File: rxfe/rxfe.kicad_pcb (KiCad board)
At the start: 2 copper layers, 117.1 x 30.7 mm, 71 parts, among them J1 SMA, J2 SMA, J3 4610X-AP1-103LF, P1 CONN_10X2, P2 CONN_2, U1 SKY12347, U10 SMP1330-005LF, U11 SMP1330-005LF, U12 SMP1330-005LF, U2 74HC04, U3 SCLF-25, U4 HMC595, U5 HMC595, U6 MGA-61563, U7 MGA-61563, U8 HMC595, U9 HMC595

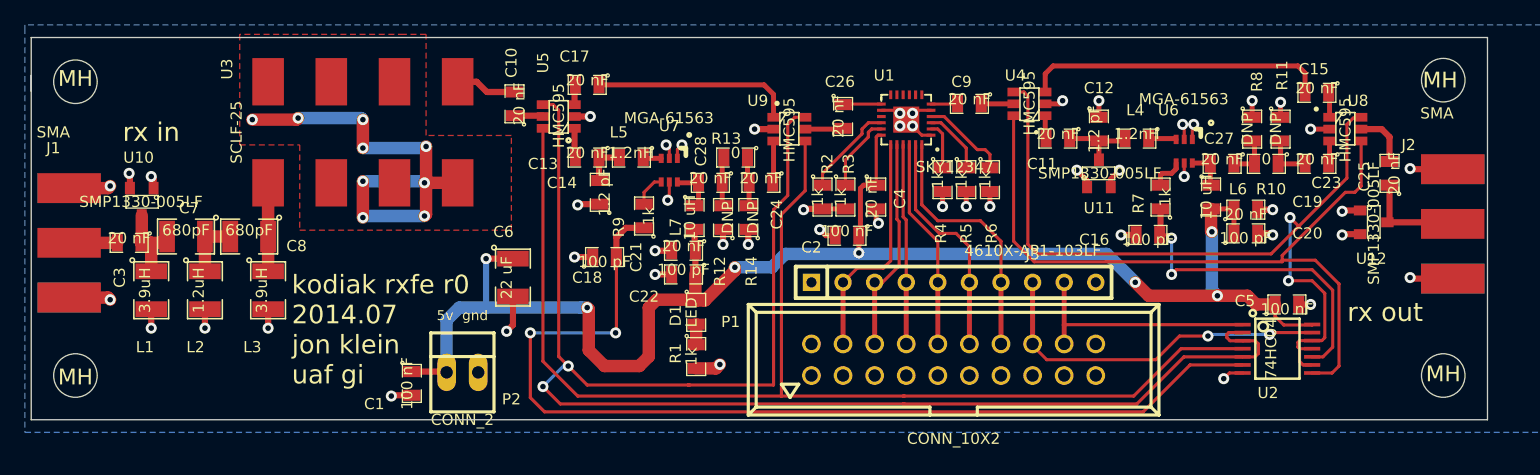
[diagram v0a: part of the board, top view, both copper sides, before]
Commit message: fixed layout bugs on rxfe, changed usrp control header, added 12v->5v linear regulator
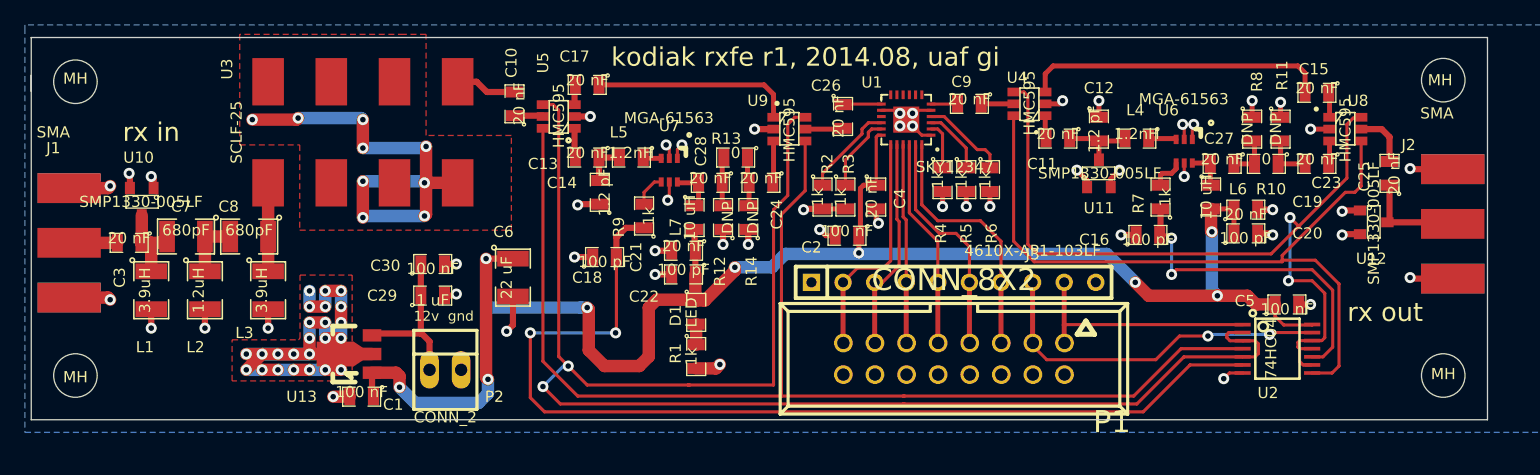
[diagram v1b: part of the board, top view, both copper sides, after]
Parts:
- added C29: 100 nF, SMD_Packages:SMD-0805, F.Cu at (131.3, 108.1)
- added C30: 1 uF, SMD_Packages:SMD-0805, F.Cu at (131.3, 110.7)
- added U13: LM7805, Housings_SOT-89:SOT89-3_Housing, F.Cu at (124.6, 115.4)
- P1: value CONN_10X2 -> CONN_8X2; footprint Connect:VASCH10x2 -> Connect:VASCH8x2
- moved C1 4.18 mm to (125.6, 118.8), turned to 180 degrees
- moved P2 1.39 mm to (132.4, 116.6)
- moved P1 0.08 mm to (173.3, 115.7), turned to 180 degrees
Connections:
- P1 pad 1: (no net) -> /AMP1CTL
- P1 pad 10: Net-(J3-Pad5) -> GND
- P1 pad 11: (no net) -> Net-(J3-Pad4)
- P1 pad 12: Net-(J3-Pad6) -> GND
- P1 pad 13: (no net) -> Net-(J3-Pad3)
- P1 pad 14: Net-(J3-Pad7) -> GND
- P1 pad 15: (no net) -> Net-(J3-Pad2)
- P1 pad 16: /AMP2CTL -> GND
- P1 pad 2: (no net) -> GND
- P1 pad 3: (no net) -> /AMP2CTL
- P1 pad 4: Net-(J3-Pad2) -> GND
- P1 pad 5: (no net) -> Net-(J3-Pad7)
- P1 pad 6: Net-(J3-Pad3) -> GND
- P1 pad 7: (no net) -> Net-(J3-Pad6)
- P1 pad 8: Net-(J3-Pad4) -> GND
- P1 pad 9: (no net) -> Net-(J3-Pad5)
- P2 pad 1: +5V -> Net-(C29-Pad1)
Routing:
- net GND: track 125.9 -> 177.4 mm, vias 59 -> 85
- net +5V: track 124.0 -> 137.5 mm, vias 7 -> 9
- net Net-(C29-Pad1): track 0.00 -> 12.9 mm
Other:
- board text added: "12v gnd"
- board text added: "kodiak rxfe r1 2014.08 jon klein uaf gi"
- board text added: "kodiak rxfe r1, 2014.08, uaf gi"
- board text removed: "5v gnd"
- board text removed: "kodiak rxfe r0 2014.07 jon klein uaf gi"

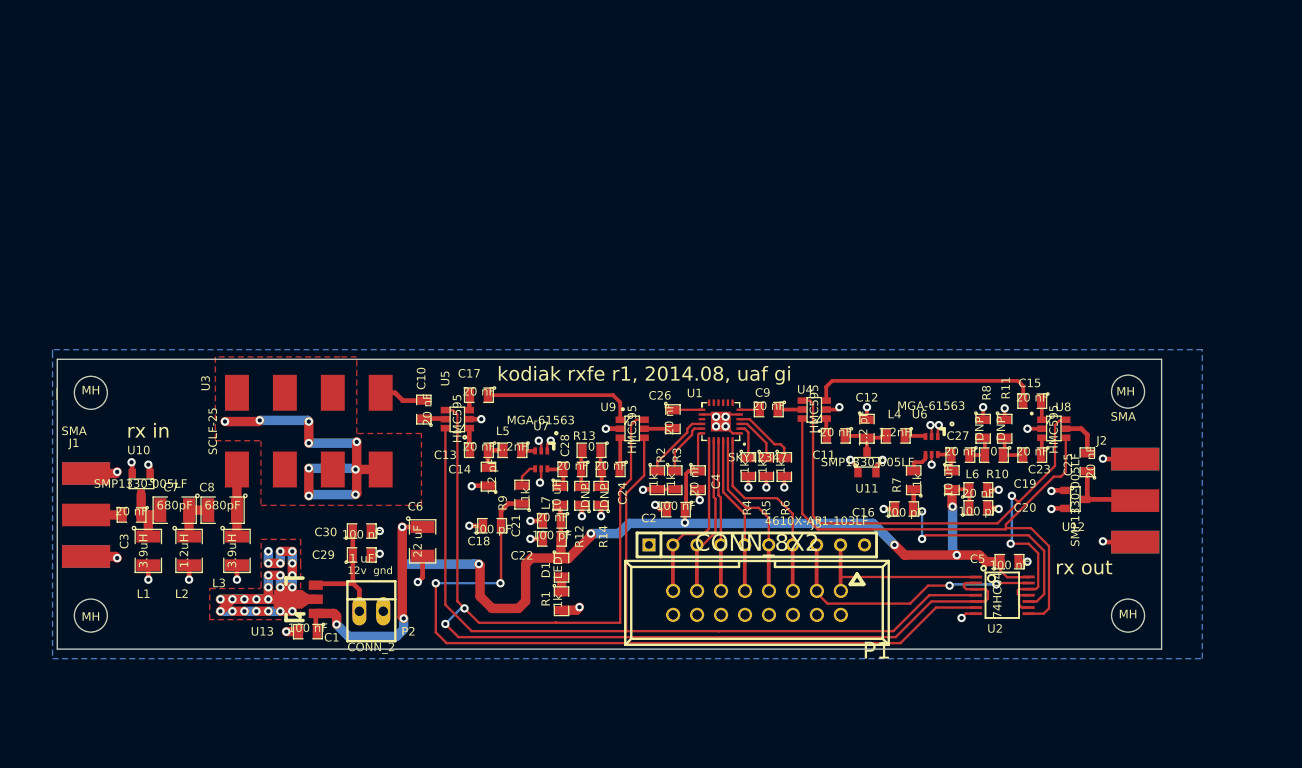
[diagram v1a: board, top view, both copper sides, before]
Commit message: switched to through hole SMA connectors on rxfe and control board, added larger mounting holes for rxfe to mount directly to shelf
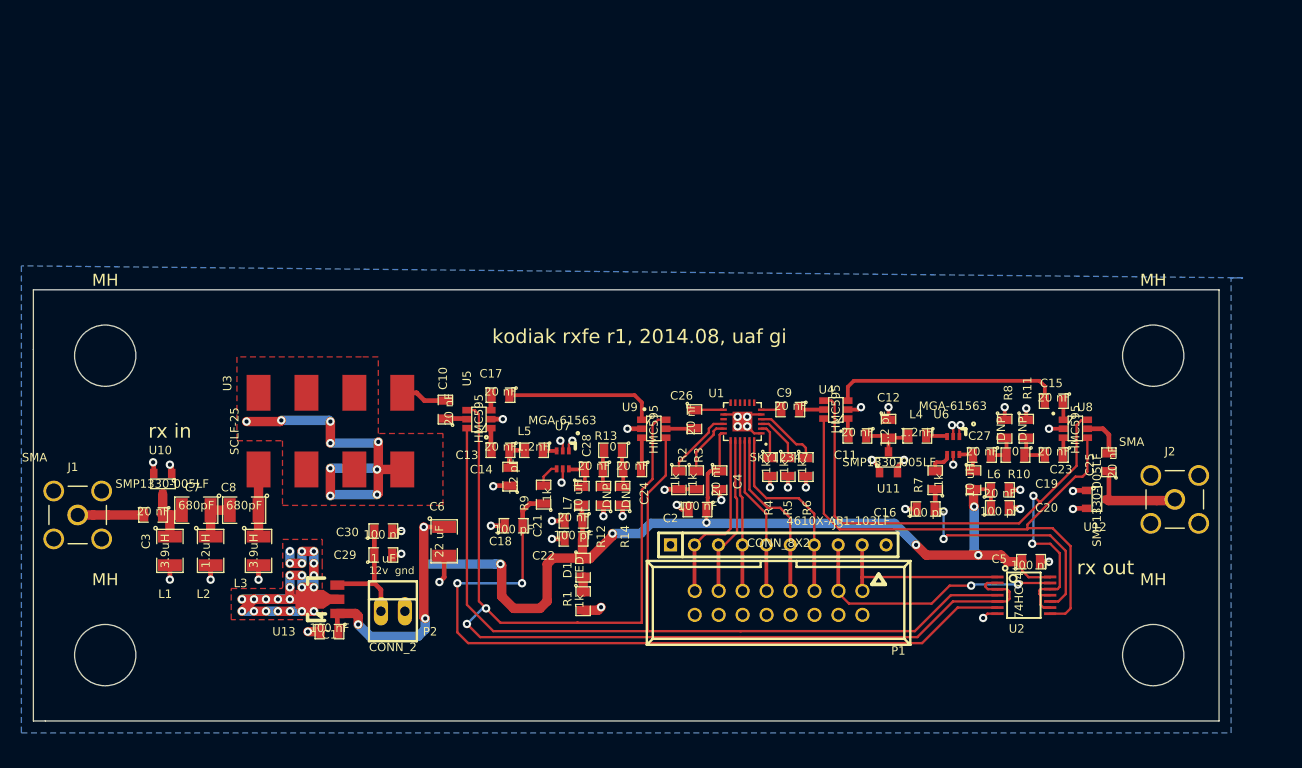
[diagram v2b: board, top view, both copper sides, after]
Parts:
- removed the MH at (212.6, 93.3)
- removed the MH at (212.6, 117.1)
- removed the MH at (102.6, 117.1)
- removed the MH at (102.6, 93.5)
- added MH: MountingHole_6-5mm_RevA_Date21Jun2010, Mounting_Holes:MountingHole_6-5mm, F.Cu at (104.1, 89.5)
- added MH: MountingHole_6-5mm_RevA_Date21Jun2010, Mounting_Holes:MountingHole_6-5mm, F.Cu at (104.1, 121.3)
- added MH: MountingHole_6-5mm_RevA_Date21Jun2010, Mounting_Holes:MountingHole_6-5mm, F.Cu at (215.3, 121.3)
- added MH: MountingHole_6-5mm_RevA_Date21Jun2010, Mounting_Holes:MountingHole_6-5mm, F.Cu at (215.3, 89.5)
- C1: footprint SMD_Packages:SM0805 -> SMD_Packages:SMD-0805
- J1, J2: footprint sma:sma -> local:SMA_5-1814832-1
- moved J2 4.19 mm to (217.6, 104.8)
- moved C1 2.29 mm to (127.9, 118.8)
- moved C10 2.29 mm to (140.2, 95.2)
- moved C12 2.29 mm to (187.2, 97.3)
- moved C13 2.29 mm to (146.1, 99.6)
- moved C14 2.29 mm to (147.1, 102.4)
- moved C15 2.29 mm to (204.7, 94.4)
- moved C16 2.29 mm to (191.1, 105.8)
- moved C17 2.29 mm to (146.1, 93.7)
- moved C18 2.29 mm to (147.4, 107.6)
- moved C2 2.29 mm to (166.9, 105.9)
- moved C21 2.29 mm to (153.8, 107.1)
- moved C22 2.29 mm to (153.8, 109.0)
- moved C23 2.29 mm to (204.7, 100.1)
- moved C24 2.29 mm to (160.0, 101.6)
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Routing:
- net GND: track 177.4 -> 163.8 mm, vias 85 -> 81
- net Net-(C3-Pad2): track 3.87 -> 7.05 mm
- net Net-(C25-Pad1): track 8.36 -> 10.3 mm
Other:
- board size 117.1 x 30.7 mm -> 125.7 x 45.7 mm

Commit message: moved mounting holes on rxfe to match shelf
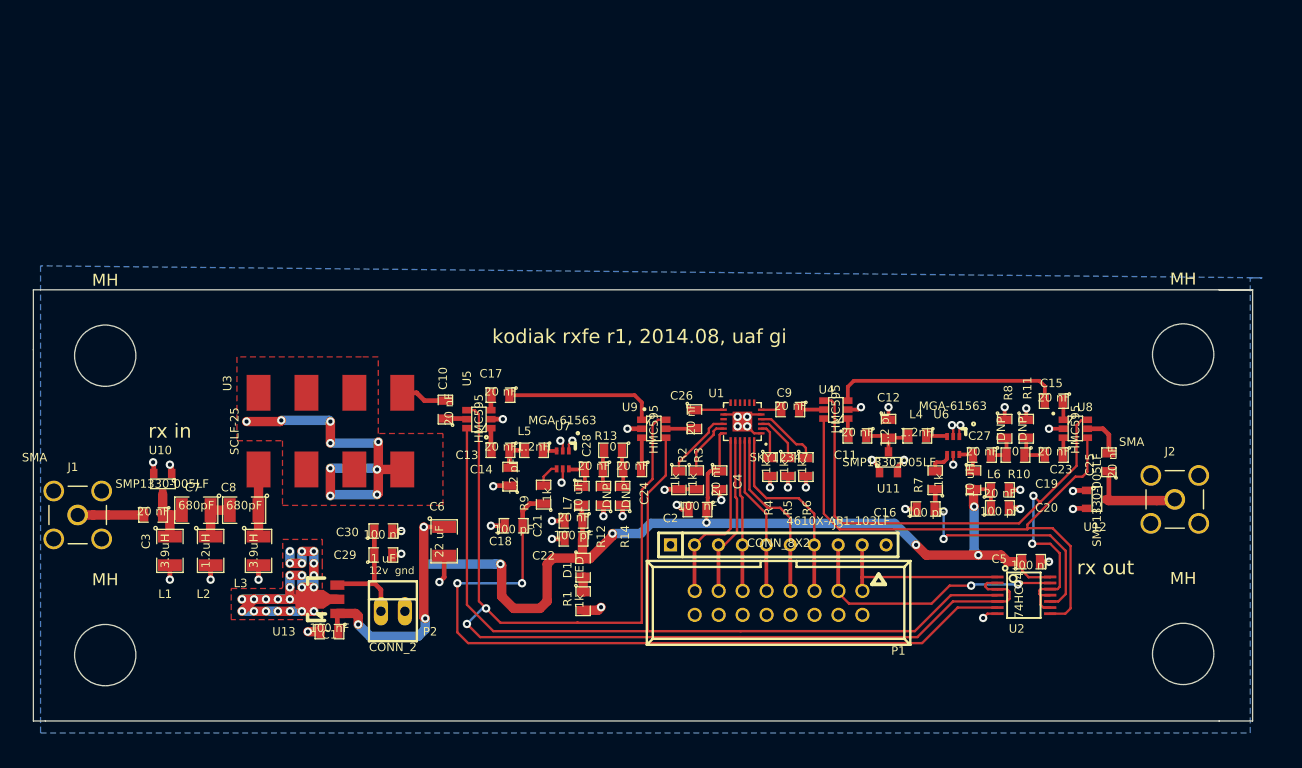
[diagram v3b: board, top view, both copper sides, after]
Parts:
- moved MH 3.18 mm to (218.4, 121.2)
- moved MH 3.18 mm to (218.4, 89.4)
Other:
- board size 125.7 x 45.7 mm -> 129.3 x 45.7 mm

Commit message: switched driver amp current limiter to to-220 lm317hv, heatsink against al plate
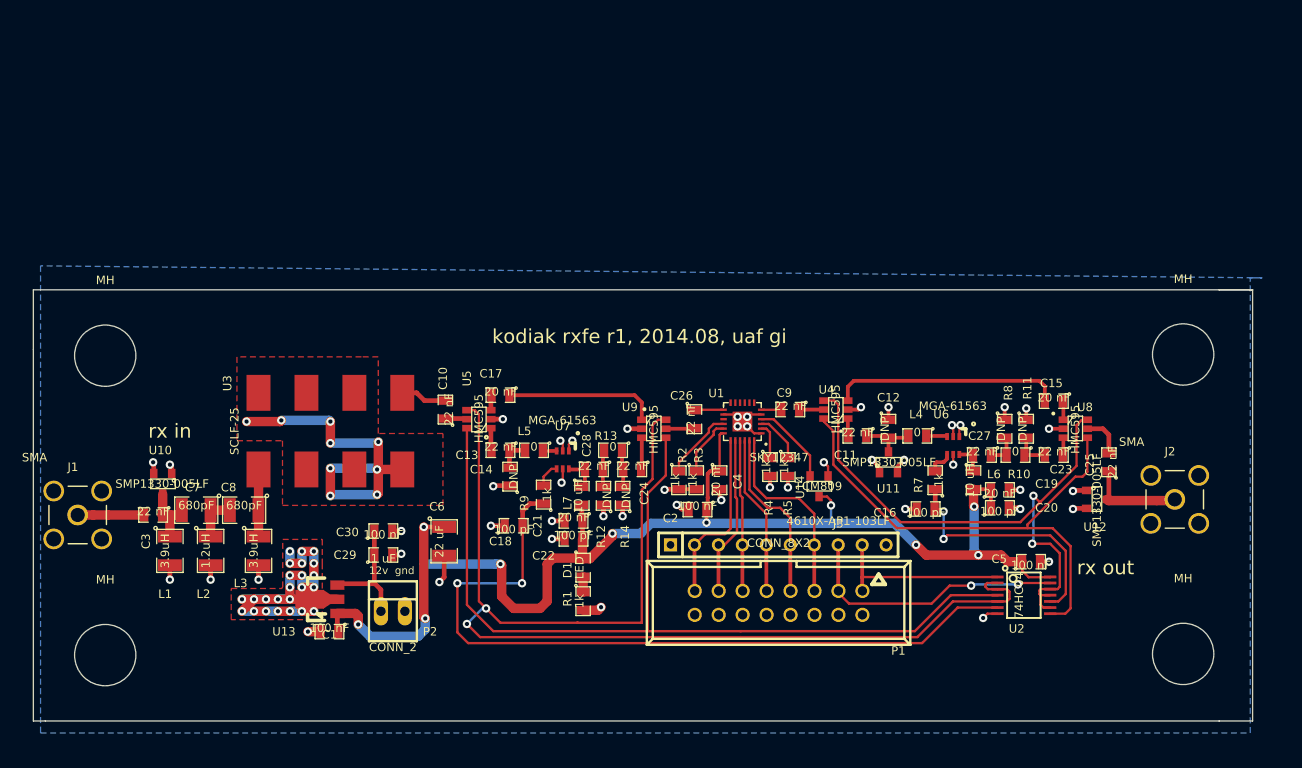
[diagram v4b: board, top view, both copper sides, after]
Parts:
- removed R6: 1k, SMD_Packages:SM0805
- added U14: TCM809, SMD_Packages:SOT-23, F.Cu at (179.8, 103.4)
- C10, C11, C13, C23, C24, C25, C26, C27, C28, C3, C9: value 20 nF -> 22 nF
- C12, C14: value 1.2 pF -> DNP
- L4, L5: value 1.2nH -> 0
- U13: value LM7805 -> 7805
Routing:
- net +5V: track 137.5 -> 141.6 mm, vias 9 -> 10
- net /AMP2: track 59.5 -> 55.7 mm
- net /~AMP2: track 66.7 -> 62.9 mm
- net Net-(U1-Pad4): track 7.07 -> 8.92 mm

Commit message: updated silkscreen on rxfe
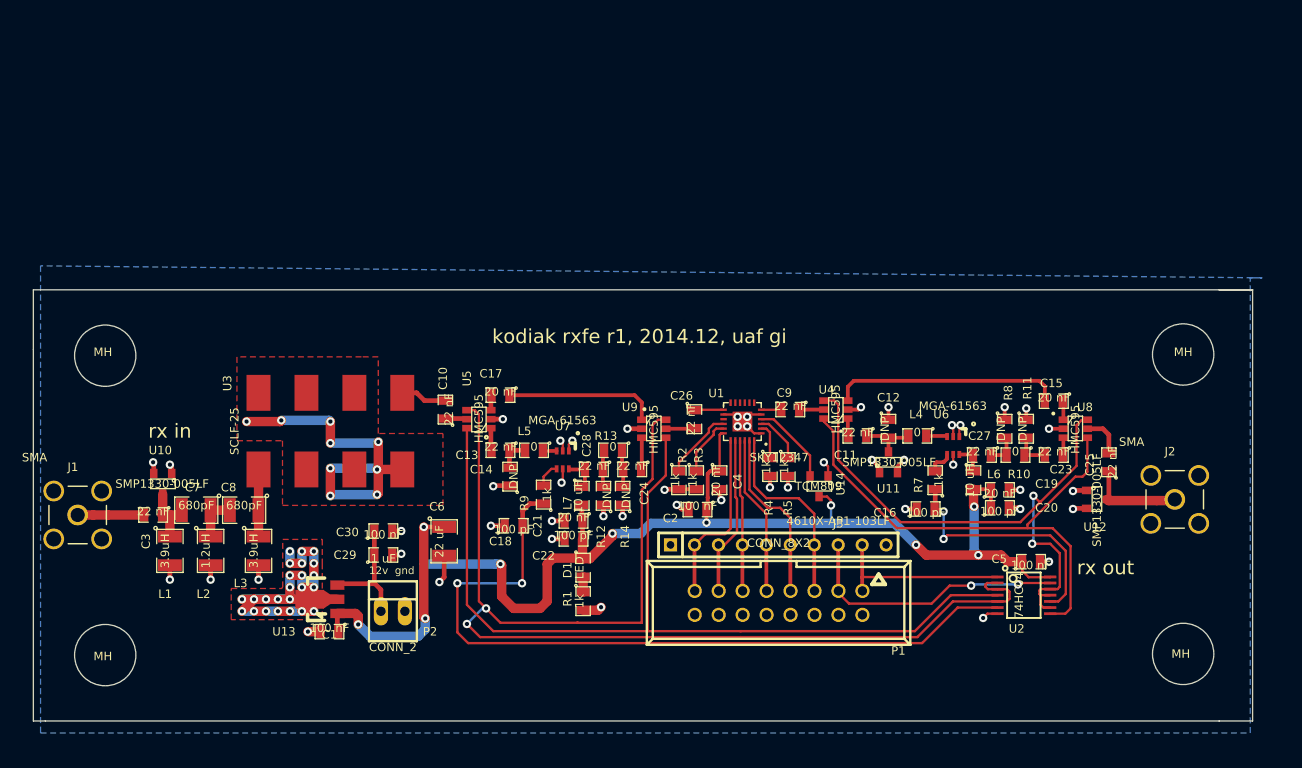
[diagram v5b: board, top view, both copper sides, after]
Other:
- board text added: "kodiak rxfe r1 2014.12 jon klein uaf gi"
- board text added: "kodiak rxfe r1, 2014.12, uaf gi"
- board text removed: "kodiak rxfe r1 2014.08 jon klein uaf gi"
- board text removed: "kodiak rxfe r1, 2014.08, uaf gi"

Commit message: moved amp from control board to rxfe
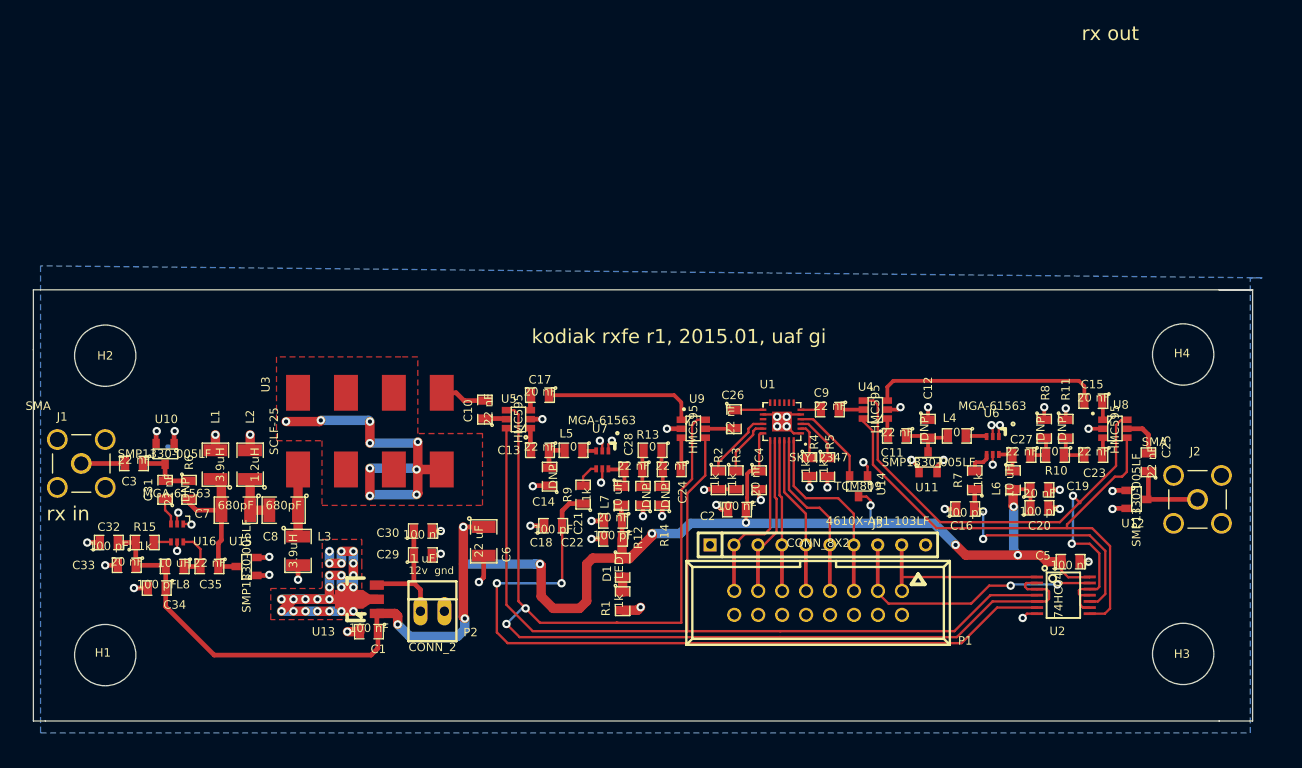
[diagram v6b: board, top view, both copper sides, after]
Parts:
- removed MH (x4): MountingHole_6-5mm_RevA_Date21Jun2010, Mounting_Holes:MountingHole_6-5mm
- added C31: 22 nF, SMD_Packages:SMD-0805, F.Cu at (110.5, 103.8)
- added C32: 100 pF, SMD_Packages:SMD-0805, F.Cu at (104.5, 109.3)
- added C33: 20 nF, SMD_Packages:SMD-0805, F.Cu at (106.4, 111.8)
- added C34: 100 pF, SMD_Packages:SMD-0805, F.Cu at (109.6, 114.2)
- added C35: 22 nF, SMD_Packages:SMD-0805, F.Cu at (115.2, 111.9)
- added H1: MOUNTING_HOLE, Mounting_Holes:MountingHole_6-5mm, F.Cu at (104.1, 121.3)
- added H2: MOUNTING_HOLE, Mounting_Holes:MountingHole_6-5mm, F.Cu at (104.1, 89.5)
- added H3: MOUNTING_HOLE, Mounting_Holes:MountingHole_6-5mm, F.Cu at (218.4, 121.2)
- added H4: MOUNTING_HOLE, Mounting_Holes:MountingHole_6-5mm, F.Cu at (218.4, 89.4)
- added L8: 10 uH, SMD_Packages:SMD-0805, F.Cu at (111.5, 111.9)
- added R15: 1k, SMD_Packages:SMD-0805, F.Cu at (108.3, 109.3)
- added R6: DNP, SMD_Packages:SMD-0805, F.Cu at (113.0, 103.8)
- added U15: SMP1330-005LF, SMD_Packages:SOT-23, F.Cu at (119.1, 111.9)
- added U16: MGA-61563, Housings_SOT-23_SOT-143_TSOT-6:SC70-6, F.Cu at (111.8, 108.3)
- C10, C11, C12, C13, C14, C15, C16, C17, C18, C19, C2, C20, C21, C22, C23, C24, C25, C26, C27, C28, C3, C4, C5, C9, D1, L4, L5, L6, L7, R1, R10, R11, R12, R13, R14, R2, R3, R4, R5, R7, R8, R9: footprint SMD_Packages:SM0805 -> SMD_Packages:SMD-0805
- C6, C7, C8, L1, L2, L3: footprint SMD_Packages:SM1210 -> SMD_Packages:SMD-1210
- U10, U11, U12: footprint SMD_Packages:SOT23 -> SMD_Packages:SOT-23
- U4, U5, U8, U9: footprint SMD_Packages:SOT23_6 -> SMD_Packages:SOT-23-6
- moved L1 10.3 mm to (115.8, 101.1), turned to 90 degrees
- moved L2 10.1 mm to (119.5, 101.1), turned to 90 degrees
- moved C3 5.83 mm to (107.2, 101.0)
- moved J1 5.47 mm to (101.6, 101.0)
- moved U13 4.19 mm to (131.1, 115.4)
- moved C1 4.19 mm to (132.1, 118.8)
- moved C10 4.19 mm to (144.4, 95.2)
- moved C11 4.19 mm to (188.1, 98.0)
- moved C12 4.19 mm to (191.4, 97.3)
- moved C13 4.19 mm to (150.2, 99.6)
- moved C14 4.19 mm to (151.3, 102.4)
- moved C15 4.19 mm to (208.9, 94.4)
- moved C16 4.19 mm to (195.3, 105.8)
- moved C17 4.19 mm to (150.2, 93.7)
- moved C18 4.19 mm to (151.6, 107.6)
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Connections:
- C7 pad 2: Net-(C3-Pad1) -> Net-(C35-Pad1)
- L1 pad 1: Net-(C3-Pad1) -> Net-(C35-Pad1)
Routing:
- net +5V: track 141.6 -> 180.1 mm
- net Net-(C35-Pad1): track 0.00 -> 16.1 mm
- net GND: track 164.2 -> 173.9 mm, vias 81 -> 89
- net Net-(C35-Pad2): track 0.00 -> 5.76 mm
- net Net-(C31-Pad1): track 0.00 -> 3.08 mm
- net Net-(C3-Pad2): track 7.05 -> 4.64 mm
- net Net-(C25-Pad1): track 10.3 -> 8.43 mm
- net Net-(R15-Pad2): track 0.00 -> 1.85 mm
- net Net-(C3-Pad1): track 7.33 -> 6.68 mm
- net Net-(C7-Pad1): track 4.83 -> 5.33 mm
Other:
- board text added: "kodiak rxfe r1 2015.01 jon klein uaf gi"
- board text added: "kodiak rxfe r1, 2015.01, uaf gi"
- board text removed: "kodiak rxfe r1 2014.12 jon klein uaf gi"
- board text removed: "kodiak rxfe r1, 2014.12, uaf gi"
